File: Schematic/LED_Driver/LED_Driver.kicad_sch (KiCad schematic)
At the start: 19 parts, among them J1 Conn_01x02, J2 DC IN 19V, U1 AL8843SP-13, U2 LM4040DYM3-2.5

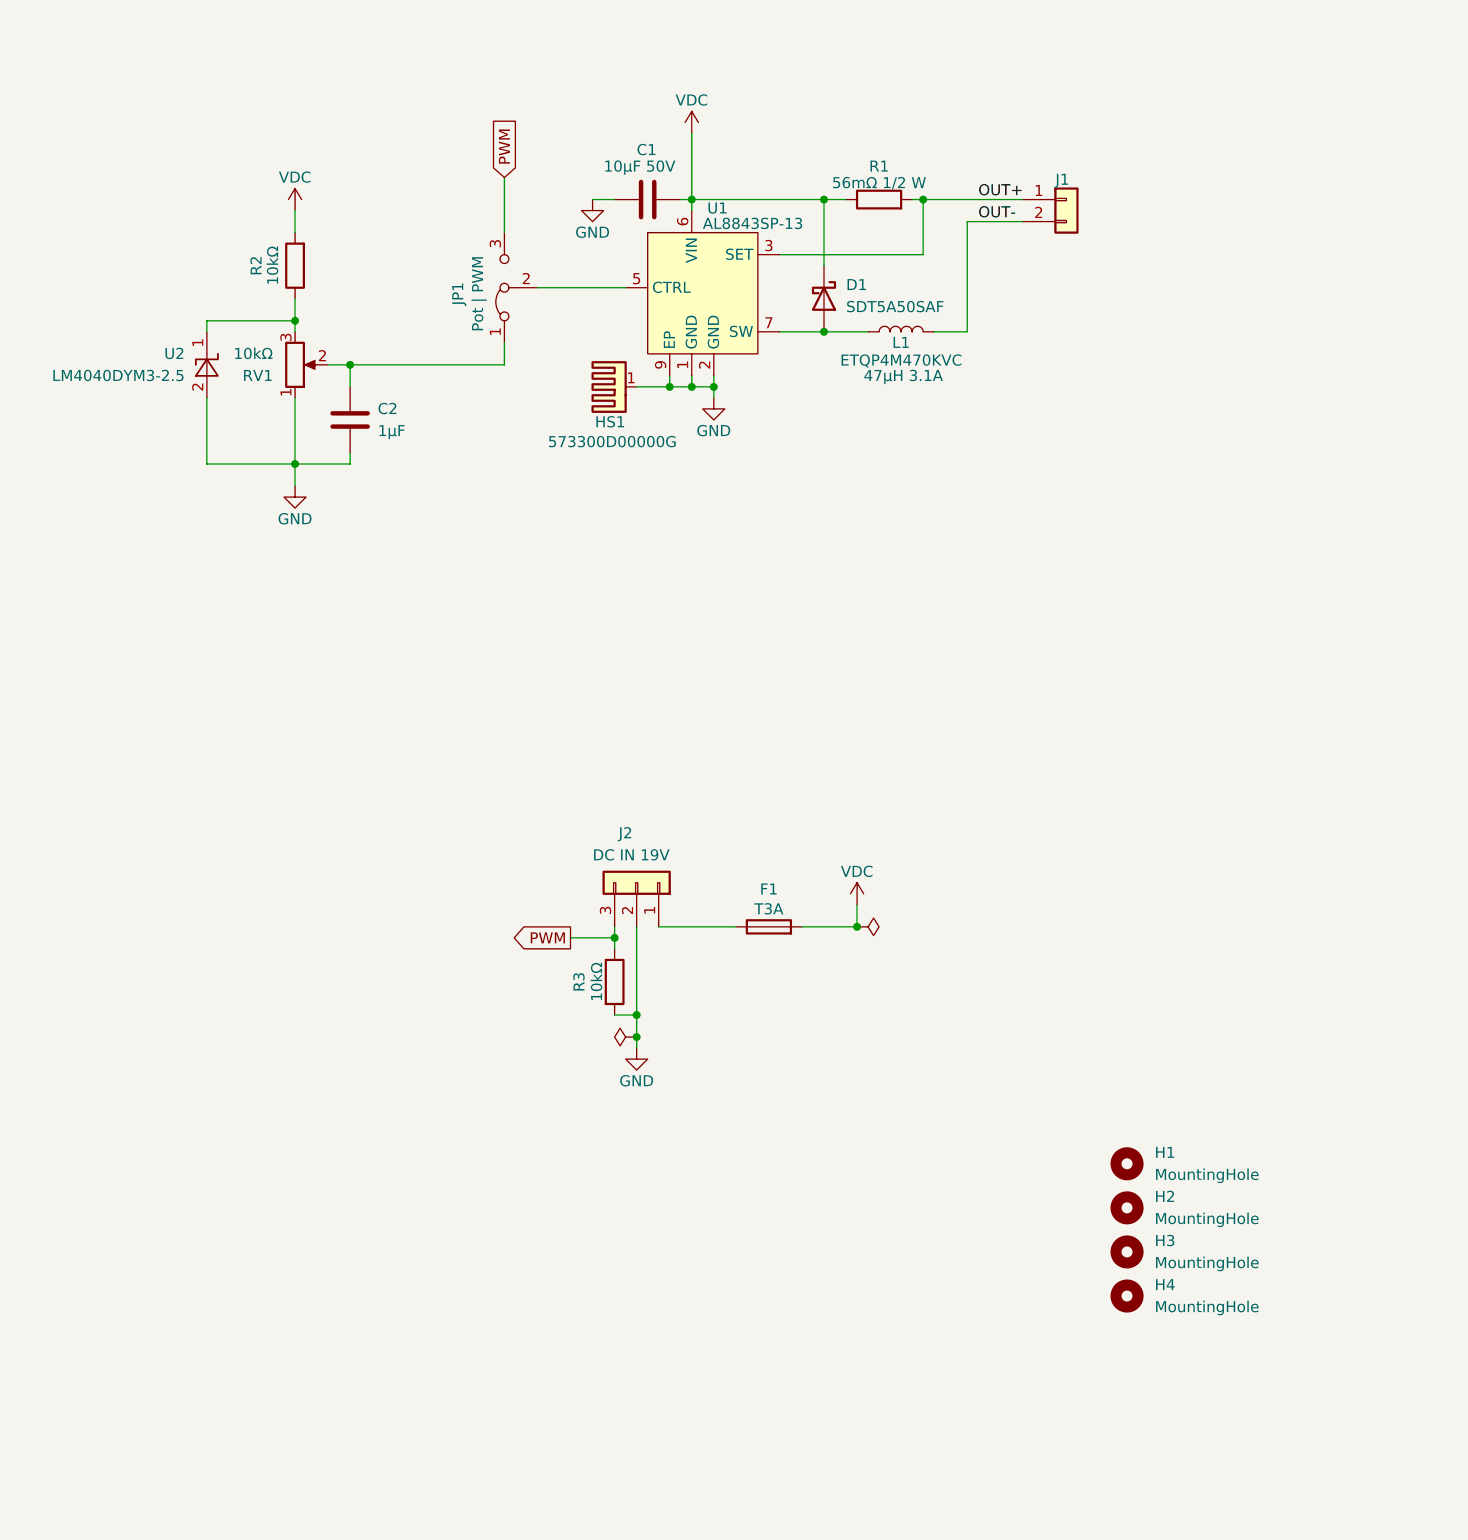
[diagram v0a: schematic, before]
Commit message: Rearranged schematic, added copy ring
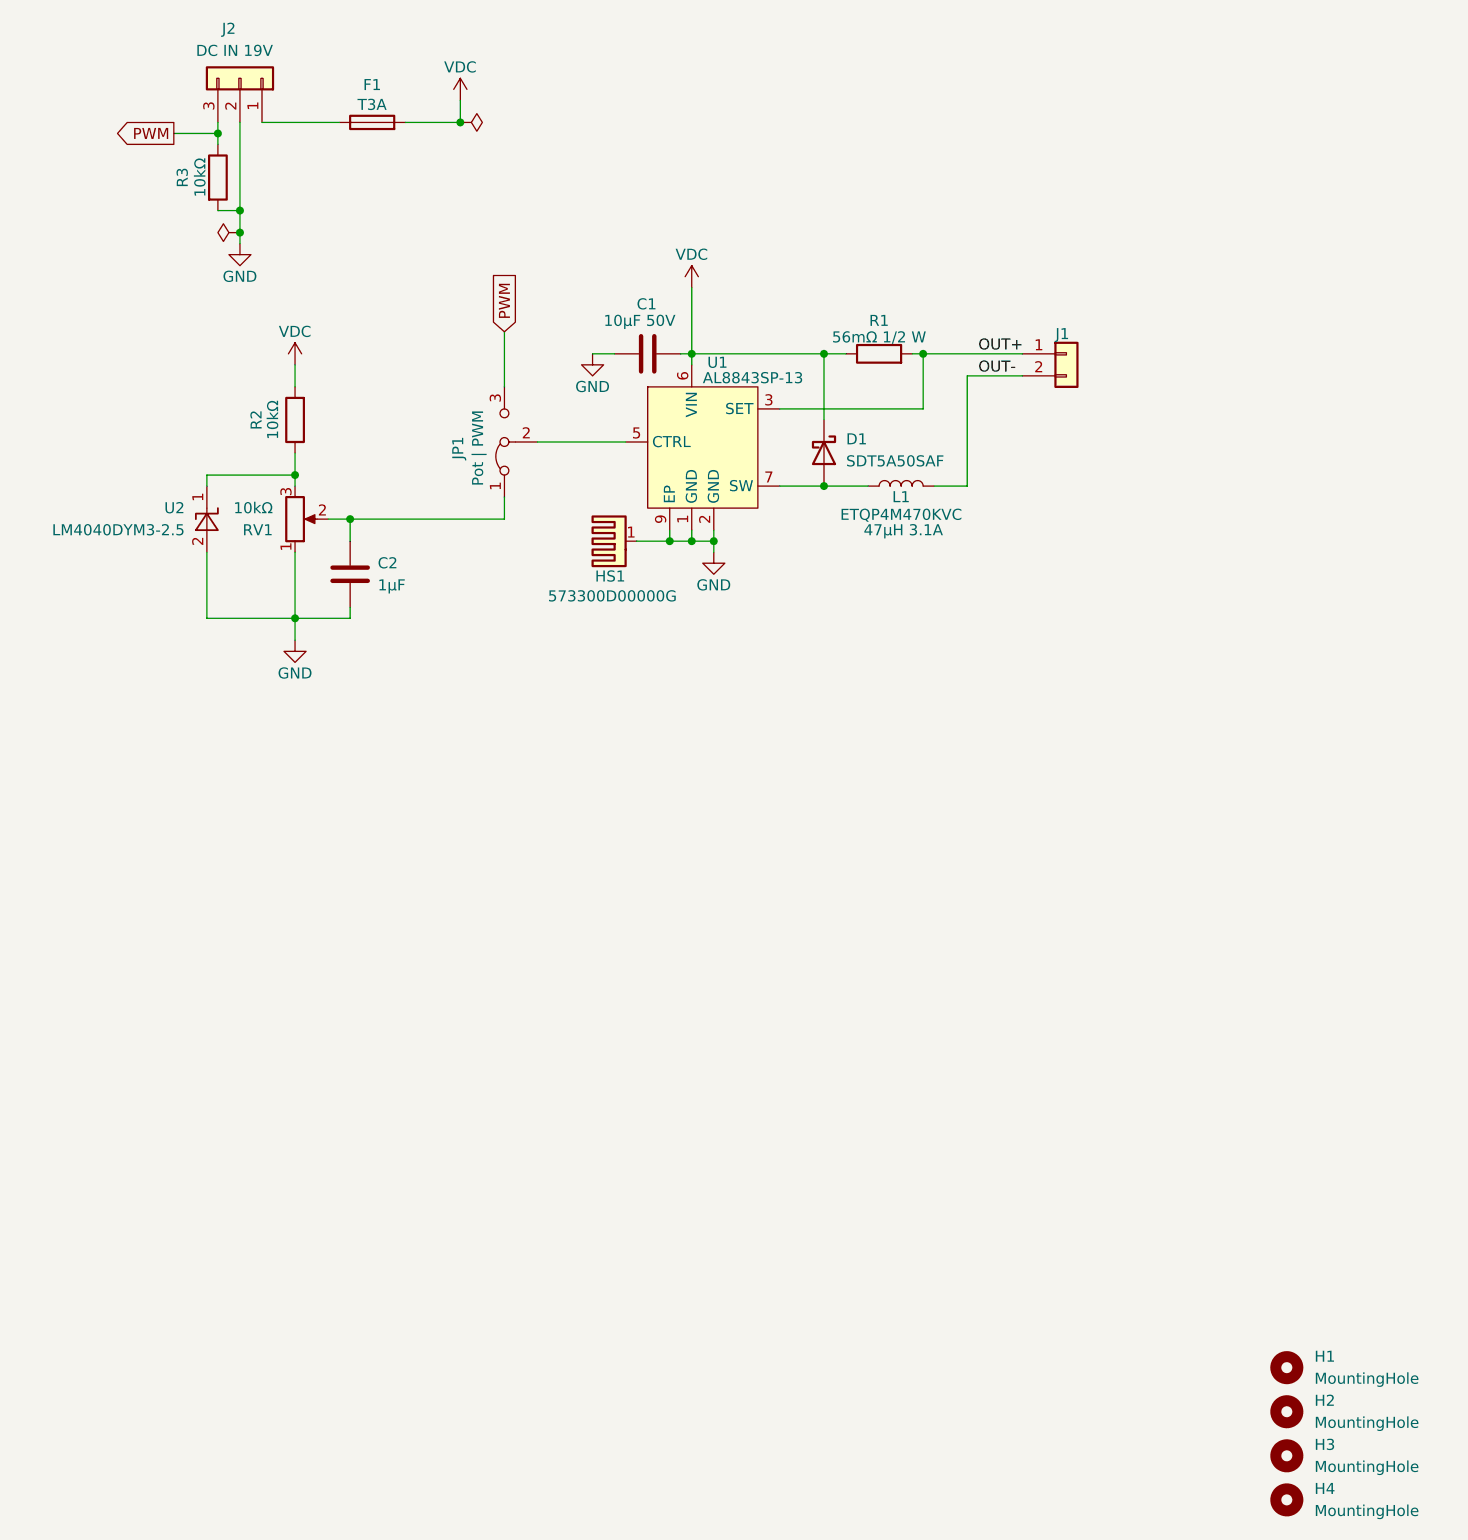
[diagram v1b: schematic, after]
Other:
- company: (none) -> Retronics - Bjørner Sandom
- title: (none) -> Horticulture LED dimmer
- moved on the sheet: C1, C2, D1, F1, H1, H2, H3, H4, HS1, J1, J2, JP1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
